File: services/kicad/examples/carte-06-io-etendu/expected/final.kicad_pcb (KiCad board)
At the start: 2 copper layers, 48.4 x 36.3 mm, 35 parts, among them J1 IN_5V, J10 IO0, J11 IO1, J2 SWD, U1 STM32F103C8T6, U2 AMS1117-3.3

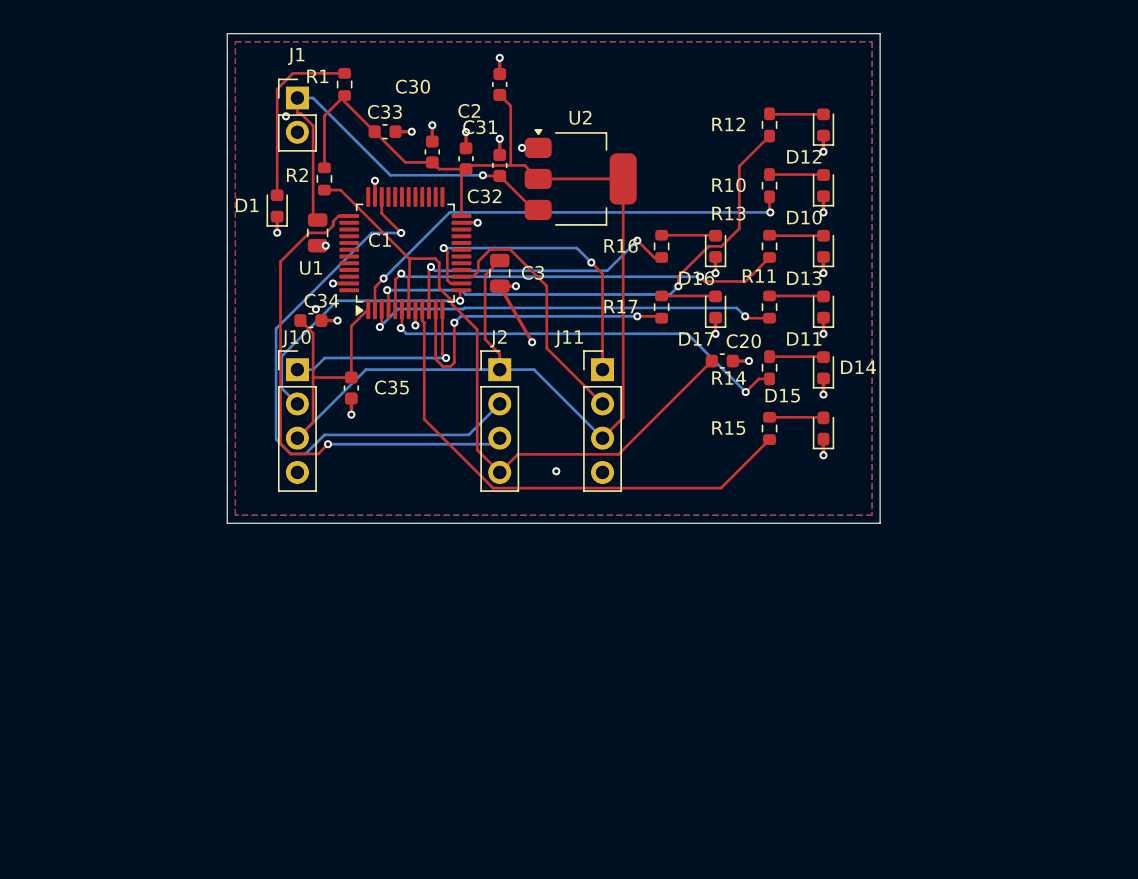
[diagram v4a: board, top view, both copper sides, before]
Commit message: fix(banc): le contour n etait JAMAIS resserre — dix cartes divisees par 2 a 4
Question de l utilisateur devant les rendus : « tu es satisfait de ce
placement ? ». Non, et la mesure lui donnait raison.

    carte-10 livree     140 x 105 mm = 14725 mm2
    son circuit          51 x  66 mm =  3366 mm2
    OCCUPATION                            23 %
    connecteurs                      56 a 75 mm du circuit
    fil de signal                      1230 mm  (VIN a lui seul 112 mm)

LA CAUSE : `run_pipeline.py` n envoyait pas `auto_size_board` a `/place/auto`.
Le resserrement du contour sur le placement existe depuis le 2026-09-13 et ne
s execute que si l appelant l autorise ; le defaut du modele est `False`.

C est le SEPTIEME levier de ce projet qui existe et que personne n appelle,
apres max_distance_mm, anchor_pin, WorkflowConfig.grid, constraints,
move_reference, bottom_up_placement et LocalRerouter.

⚠️ Et il etait INVISIBLE : la chaine de PRODUCTION passe bien le drapeau depuis
`handlePlacement`. Le banc mesurait donc un comportement que le produit n a
pas — l inverse exact de ce a quoi sert un banc.

MESURE APRES CORRECTION, meme circuit, meme graine :

    carte             demandee      REELLE        err  manq
    carte-01           25 x 20     20,1 x 14,6     0    0
    carte-02           55 x 40     34,9 x 25,4     0    0
    carte-03           50 x 35     26,1 x 20,1     0    0
    carte-04           60 x 45     36,6 x 27,2     0    0
    carte-05           70 x 50     43,6 x 32,6     0    0
    carte-06           80 x 60     48,5 x 36,4     0    0
    carte-07          110 x 80     53,2 x 38,8     0    0
    carte-08          125 x 95     56,4 x 44,1     0    0
    carte-09          130 x 100    57,3 x 45,2     0    0
    carte-10          140 x 105    61,0 x 45,8     0    0

Dix sur dix, 100 % route, aucune erreur, aucune connexion manquante. Sur
carte-10 : occupation 23 -> 56 %, fil de signal 1230 -> 652 mm, VIN 112 -> 45,5,
connecteurs 56-75 -> 23-35 mm.

ET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
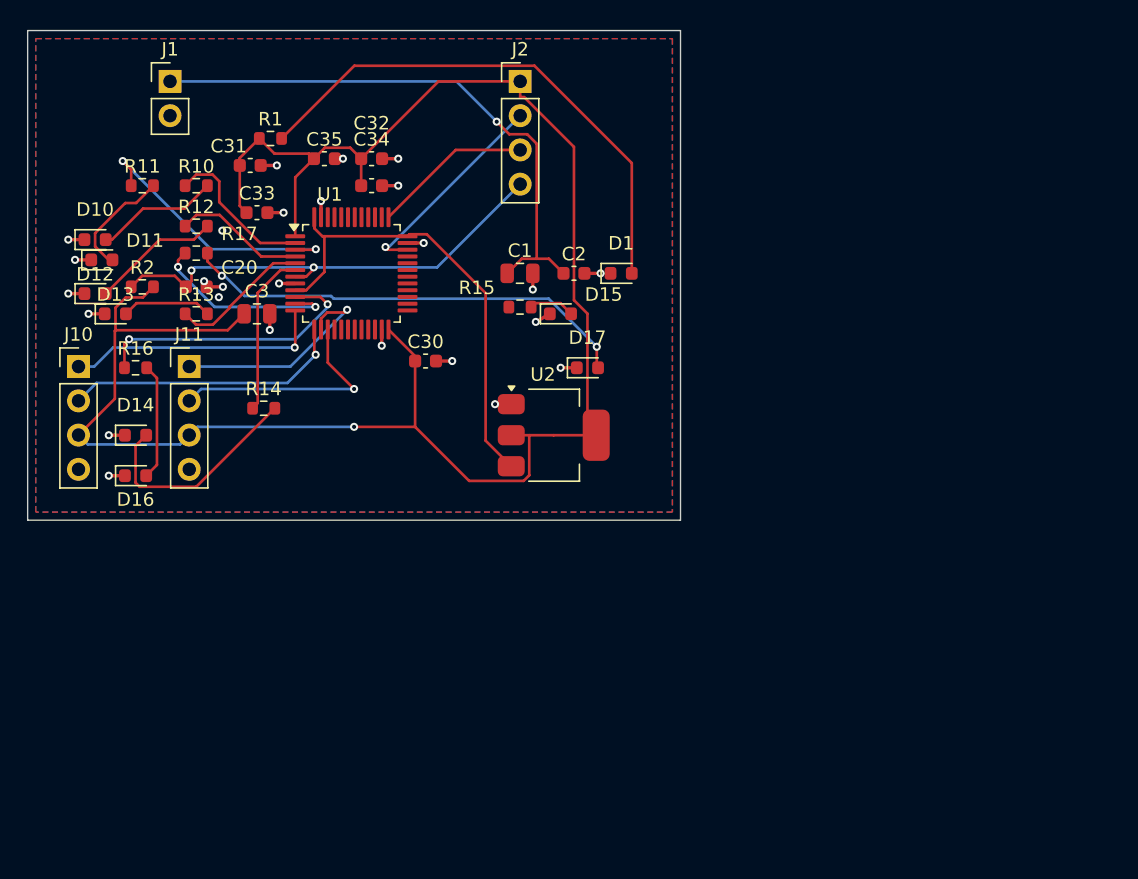
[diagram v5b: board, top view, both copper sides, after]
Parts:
- moved D12 55.4 mm to (113.5, 94.5), turned to 0 degrees
- moved D10 54.1 mm to (113.5, 90.5), turned to 0 degrees
- moved D11 53.6 mm to (114.0, 92.0), turned to 0 degrees
- moved D13 52.7 mm to (115.0, 96.0), turned to 0 degrees
- moved D14 51.2 mm to (116.5, 105.0), turned to 0 degrees
- moved R11 47.4 mm to (117.0, 86.5), turned to 0 degrees
- moved D16 46.2 mm to (116.5, 108.0), turned to 0 degrees
- moved R12 43.2 mm to (121.0, 89.5), turned to 0 degrees
- moved R13 42.8 mm to (121.0, 96.0), turned to 0 degrees
- moved R10 42.5 mm to (121.0, 86.5), turned to 0 degrees
- moved R16 40.0 mm to (116.5, 100.0), turned to 0 degrees
- moved C20 39.4 mm to (121.0, 94.0)
- moved R14 37.6 mm to (126.0, 103.0), turned to 0 degrees
- moved R17 34.7 mm to (121.0, 91.5), turned to 0 degrees
- moved J11 30.6 mm to (120.5, 99.9)
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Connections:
- U1 pad 36: Net-(U1-36) -> PWR_FLAG
- U1 pad 48: Net-(U1-48) -> PWR_FLAG
- U1 pad 9: IO_L5 -> PWR_FLAG
- U2 pad 3: VIN -> PWR_FLAG
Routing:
- net IO_L5: track 37.4 -> 0.00 mm
- net PWR_FLAG: track 0.00 -> 34.6 mm
- net +3V3: track 112.4 -> 143.8 mm, vias 0 -> 1
- net LEDA7: track 4.02 -> 33.7 mm, vias 0 -> 2
- net IO_L2: track 37.9 -> 9.78 mm, vias 2 -> 0
- net SWDIO: track 42.3 -> 15.7 mm
- net LED_PWR: track 13.4 -> 39.4 mm
- net SWCLK: track 37.2 -> 11.8 mm, vias 1 -> 0
- net IO_L0: track 34.4 -> 11.5 mm, vias 2 -> 0
- net IO_L3: track 31.1 -> 10.4 mm, vias 2 -> 0
- net IO_L4: track 31.1 -> 12.2 mm, vias 2 -> 0
- net NRST: track 51.1 -> 34.9 mm, vias 0 -> 2
- net LEDA4: track 4.02 -> 16.7 mm
- net VIN: track 31.1 -> 42.7 mm
- net IO_L1: track 31.2 -> 20.7 mm
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
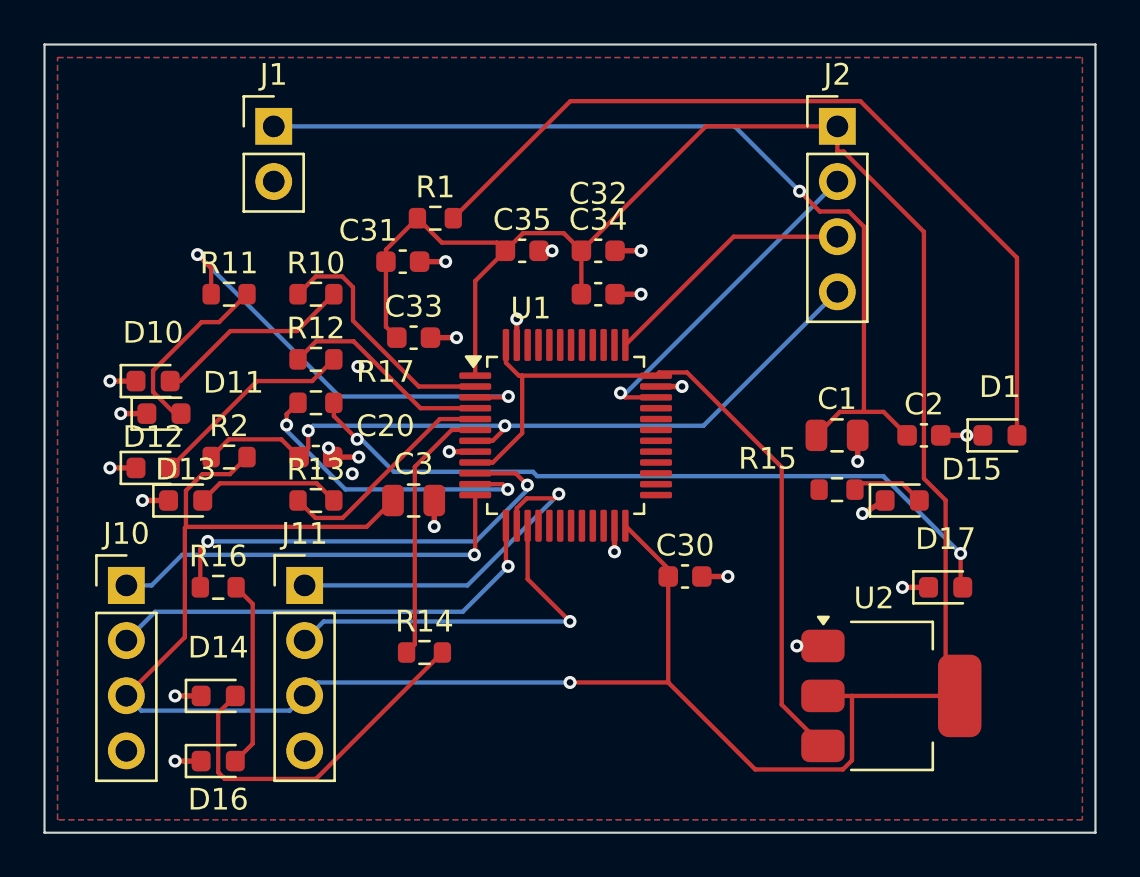
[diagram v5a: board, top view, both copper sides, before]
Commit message: feat(placement): les peripheriques se REPARTISSENT, ils ne s empilent plus
Question de l utilisateur devant le rendu : « c est quoi ce type de placement ? ».
Les composants s entassaient d un seul cote du boitier, etiquettes de
serigraphie l une sur l autre, trois quarts de la couronne vides.

TROIS CAUSES, toutes dans `_poser_les_peripheriques`, toutes la meme faute —
un angle unique pour tout un groupe :

  - les DIRECTS qui visent la meme broche (tous les decouplages d un rail,
    toutes les resistances d un meme signal) recevaient le MEME `angle_vers`
    et le meme rayon de depart ;
  - les SUIVEURS d un meme parent recevaient tous atan2(parent - centre) ;
  - les ISOLES partaient tous de l angle 0.0, c est-a-dire du meme point.

`le_long_du_rayon` ne s ecartait qu une fois la place prise : d ou la file.

REMEDE : `_ecart_en_eventail`. Le PREMIER de chaque groupe garde EXACTEMENT la
direction calculee — c est la topologie, on ne la perd pas pour faire joli — et
les suivants s ecartent symetriquement de 3 x `_PAS_ANGLE_DEG`.
Rien de deja pose ne bouge : seul l ANGLE DE DEPART de la recherche change, et
`le_long_du_rayon` reste seul juge de ce qui est libre.

BANC DES DIX CARTES, contour resserre ET peripheriques repartis :

    carte             demandee    livree         err  manq
    carte-01           25 x 20    20,1 x 13,6     0    0
    carte-02           55 x 40    34,9 x 25,2     0    0
    carte-03           50 x 35    27,6 x 19,9     0    0
    carte-04           60 x 45    36,6 x 29,8     0    0
    carte-05           70 x 50    40,0 x 32,6     0    0
    carte-06           80 x 60    46,5 x 36,4     0    0
    carte-07          110 x 80    47,7 x 38,8     0    0
    carte-08          125 x 95    57,4 x 44,1     0    0
    carte-09          130 x 100   57,8 x 45,2     0    0
    carte-10          140 x 105   59,0 x 45,8     0    0

Dix sur dix, 100 % route. carte-07 gagne 5,5 mm de largeur sur le passage
precedent, carte-06 deux, carte-10 deux. Sur ca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
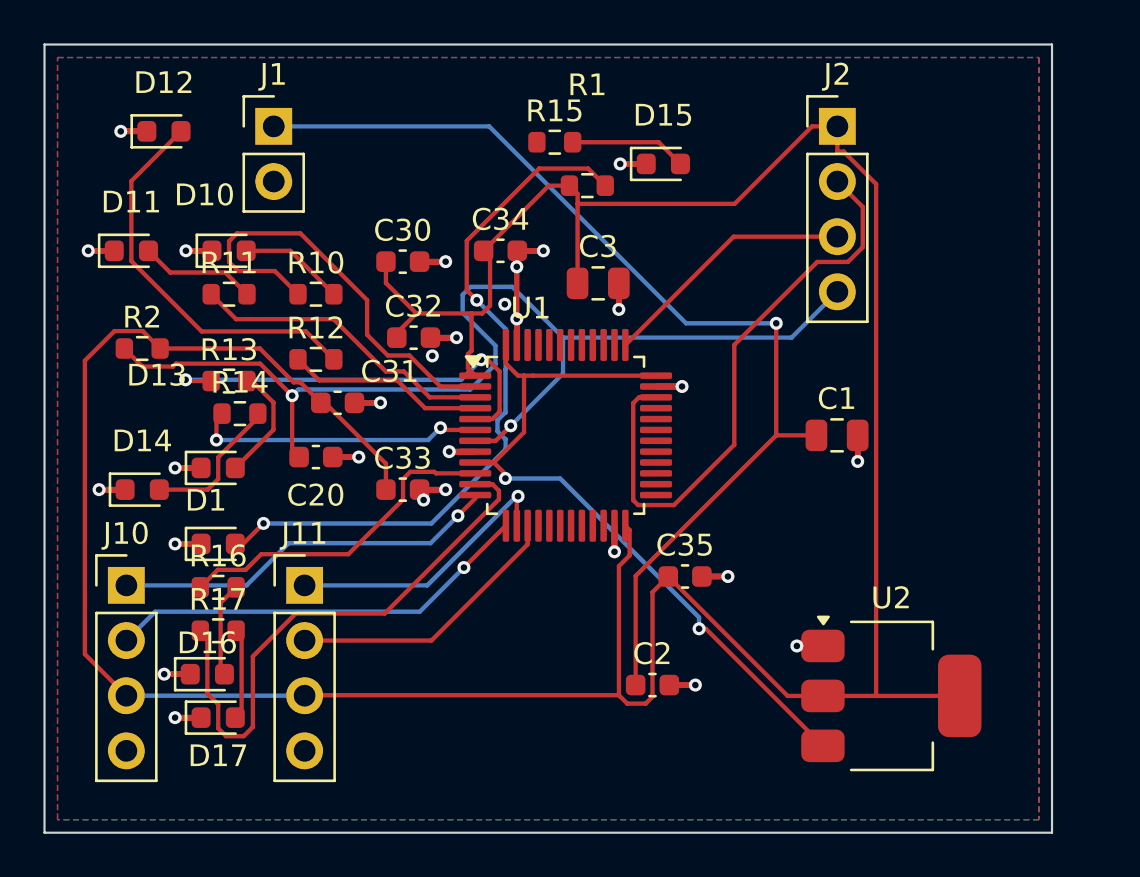
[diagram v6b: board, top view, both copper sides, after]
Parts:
- moved D1 36.3 mm to (116.5, 98.0)
- moved D17 34.0 mm to (116.5, 106.0)
- moved R15 20.6 mm to (132.0, 79.5)
- moved C30 19.5 mm to (125.0, 85.0)
- moved D15 19.0 mm to (137.0, 80.5)
- moved C2 17.0 mm to (136.5, 104.5)
- moved C35 16.8 mm to (138.0, 99.5)
- moved D12 15.5 mm to (114.0, 79.0)
- moved R14 13.9 mm to (117.5, 92.0)
- moved C3 13.1 mm to (134.0, 86.0)
- moved R17 11.4 mm to (116.5, 102.0)
- moved D14 10.1 mm to (113.0, 95.5)
- moved C32 8.73 mm to (125.5, 88.5)
- moved D11 7.65 mm to (112.5, 84.5)
- moved C31 7.16 mm to (122.0, 91.5)
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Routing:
- net GND: track 27.0 -> 94.8 mm, vias 26 -> 28
- net LEDA7: track 33.7 -> 4.22 mm, vias 2 -> 0
- net NRST: track 34.9 -> 51.7 mm
- net SWDIO: track 15.7 -> 27.4 mm, vias 1 -> 0
- net IO_L7: track 14.4 -> 25.9 mm, vias 2 -> 0
- net LEDA4: track 16.7 -> 6.68 mm
- net IO_L3: track 10.4 -> 19.4 mm, vias 0 -> 2
- net +3V3: track 143.8 -> 152.7 mm, vias 1 -> 0
- net IO_L0: track 11.5 -> 20.1 mm
- net LEDA2: track 9.61 -> 18.1 mm
- net IO_L1: track 20.7 -> 14.1 mm, vias 2 -> 0
- net LED_PWR: track 39.4 -> 33.0 mm, vias 0 -> 2
- net VIN: track 42.7 -> 48.1 mm
- net IO_L6: track 20.8 -> 15.4 mm, vias 2 -> 0
- net EXT1_2: track 17.8 -> 13.0 mm, vias 1 -> 0
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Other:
- board size 48.4 x 36.3 mm -> 46.4 x 36.3 mm

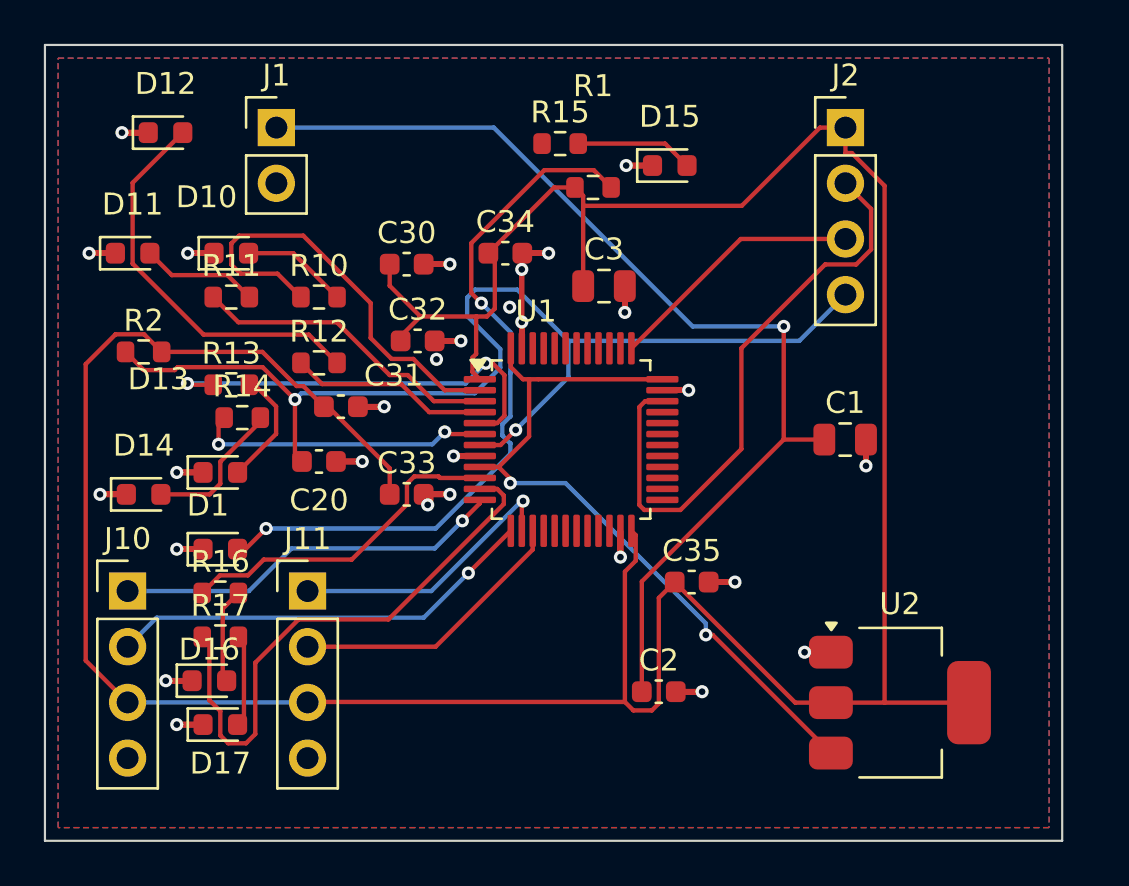
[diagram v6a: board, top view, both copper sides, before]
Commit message: docs(banc): les dix boards du banc du 2026-09-23, service corrige
Artefacts du banc dont le tableau est deja commite : les dix cartes a
100 % route, 0 erreur, 0 connexion manquante, chacune a la taille de son
circuit.

Co-Authored-By: Claude Opus 5 <noreply@anthropic.com>
Claude-Session: https://claude.ai/code/session_01TnMqm4La2CxQHHB5K8aSSV
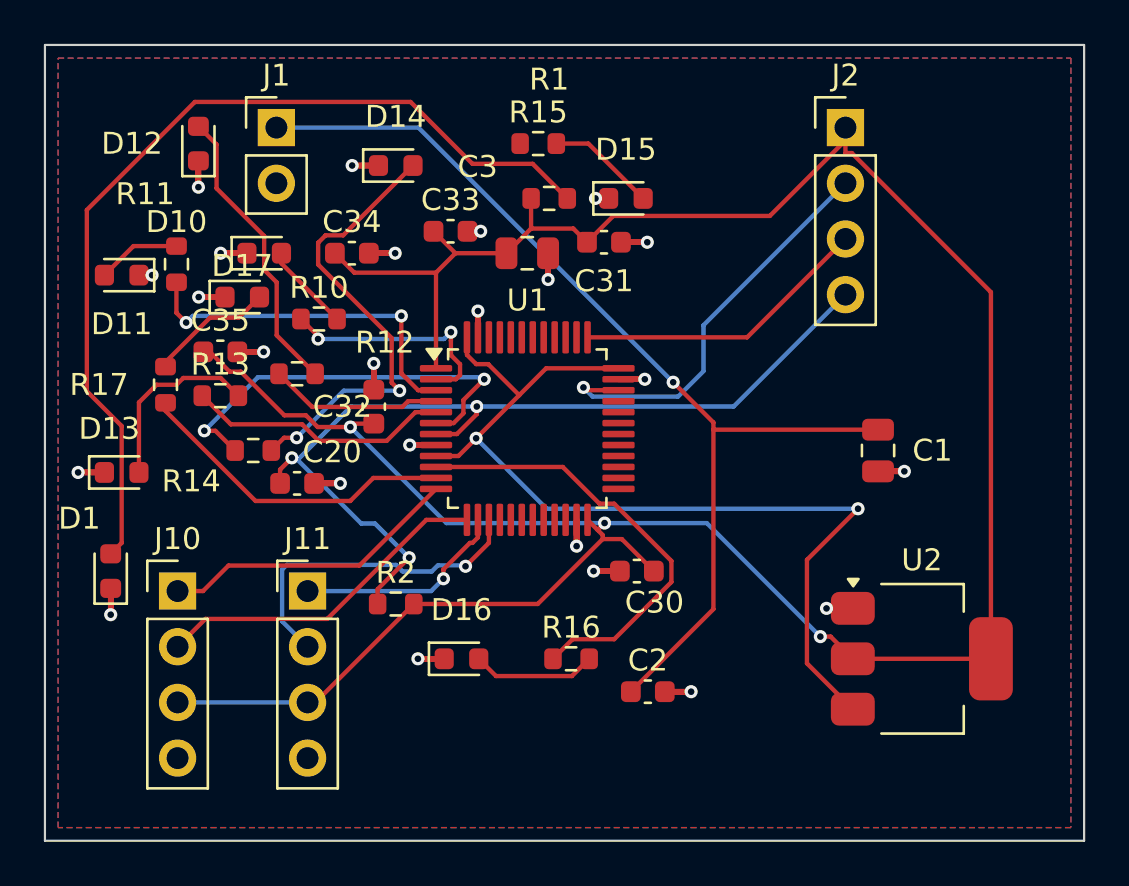
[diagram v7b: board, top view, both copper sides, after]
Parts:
- moved C35 23.9 mm to (116.5, 89.0)
- moved D17 19.5 mm to (117.5, 86.5)
- moved D14 18.9 mm to (124.5, 80.5)
- moved C30 17.5 mm to (135.5, 99.0), turned to 180 degrees
- moved R16 16.3 mm to (132.5, 103.0)
- moved R2 16.3 mm to (124.5, 100.5)
- moved C31 14.2 mm to (134.0, 84.0)
- moved C33 12.2 mm to (127.0, 83.5)
- moved R17 11.8 mm to (114.0, 90.5), turned to 90 degrees
- moved D16 11.5 mm to (127.5, 103.0)
- moved C34 7.00 mm to (122.5, 84.5)
- moved D1 5.10 mm to (111.5, 99.0), turned to 90 degrees
- moved D13 4.50 mm to (112.0, 94.5)
- moved C3 3.81 mm to (130.5, 84.5)
- moved C32 3.61 mm to (123.5, 91.5), turned to 90 degrees
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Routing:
- net +3V3: track 152.7 -> 130.9 mm, vias 0 -> 3
- net LEDA4: track 6.68 -> 21.1 mm, vias 0 -> 2
- net IO_L7: track 25.9 -> 14.8 mm
- net NRST: track 51.7 -> 42.0 mm, vias 2 -> 3
- net IO_L0: track 20.1 -> 10.7 mm, vias 0 -> 2
- net LED_PWR: track 33.0 -> 42.3 mm, vias 2 -> 0
- net PWR_FLAG: track 34.4 -> 43.7 mm
- net SWDIO: track 27.4 -> 19.0 mm, vias 0 -> 1
- net GND: track 94.8 -> 87.0 mm, vias 28 -> 24
- net IO_L3: track 19.4 -> 12.1 mm, vias 2 -> 0
- net IO_L4: track 13.5 -> 19.0 mm
- net IO_L6: track 15.4 -> 20.3 mm
- net LEDA2: track 18.1 -> 13.5 mm
- net EXT0_1: track 17.9 -> 13.7 mm, vias 1 -> 0
- net EXT0_2: track 19.7 -> 15.6 mm, vias 1 -> 0
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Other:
- board size 46.4 x 36.3 mm -> 47.4 x 36.3 mm
